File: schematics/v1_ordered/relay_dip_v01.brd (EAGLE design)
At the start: 50 x 50 mm, 49 parts, among them IC2 DS2432P

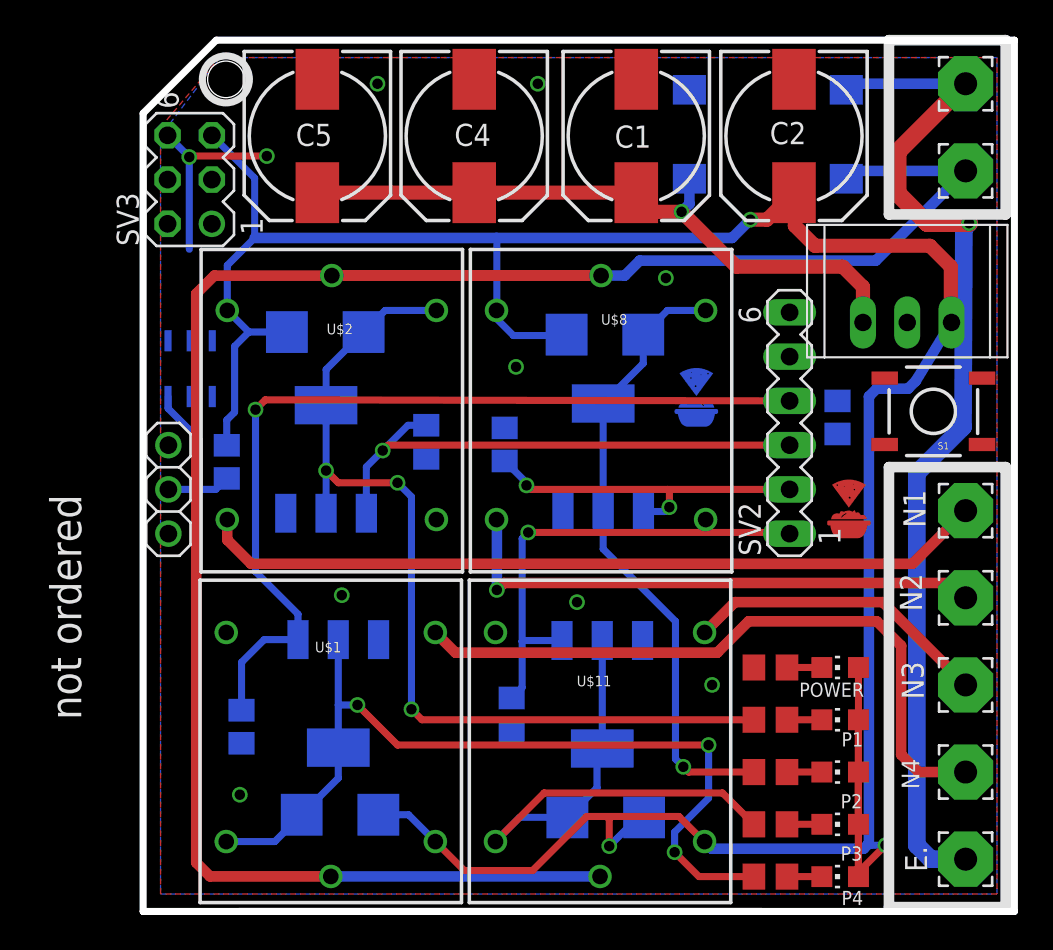
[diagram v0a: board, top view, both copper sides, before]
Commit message: moved files to subfolder
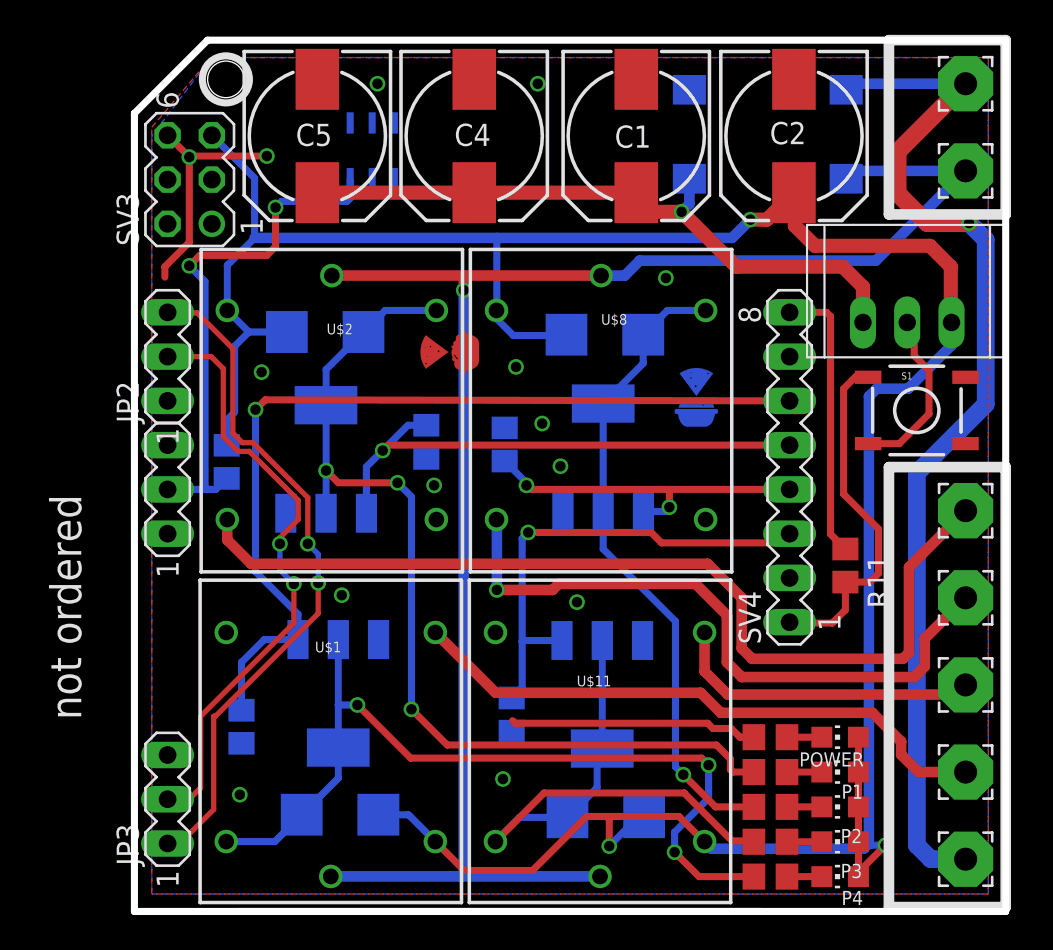
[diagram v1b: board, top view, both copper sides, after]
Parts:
- removed SV2: (no value), con-lstb:MA06-1
- added JP2, JP3: (no value), con-lstb:MA03-1
- added SV4: (no value), con-lstb:MA08-1
- JP1: device adafruit:1X03 -> con-lstb:MA03-1
- moved U$4 24.6 mm to (17.6, 32.1), turned to 90 degrees
- moved U$5 20.8 mm to (28.4, 48.0), turned to 270 degrees
- moved IC2 16.3 mm to (13.2, 43.6)
- moved R11 8.51 mm to (40.3, 19.9), flipped to the top, turned to 270 degrees
- moved POWER 4.00 mm to (40.0, 10.0)
- moved R7 4.00 mm to (36.0, 10.0)
- moved P1 3.00 mm to (40.0, 8.00)
- moved R3 3.00 mm to (36.0, 8.00)
- moved P2 2.00 mm to (40.0, 6.00)
- moved R4 2.00 mm to (36.0, 6.00)
- moved P3 1.00 mm to (40.0, 4.00)
- moved R5 1.00 mm to (36.0, 4.00)
- moved S1 0.95 mm to (44.4, 28.8), turned to 0 degrees
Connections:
- new net N$1: R11.2, S1.1, SV4.1
- new net N$6: R11.1, SV4.8
- new net SCL: JP2.2, JP3.2
- new net SDA: JP2.3, JP3.1
- net GND: now also JP3.3, S1.3
- net P0: now also SV4.6; no longer SV2.4
- net P2: now also SV4.5; no longer SV2.3
- net P4: now also SV4.4; no longer SV2.2
- net P6: now also SV4.3; no longer SV2.1
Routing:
- net SDA: track 0.00 -> 39.4 mm, vias 0 -> 2
- net SCL: track 0.00 -> 34.8 mm, vias 0 -> 2
- net PHASE: track 125.7 -> 95.9 mm, vias 0 -> 1
- net GND: track 11.6 -> 38.0 mm, vias 10 -> 14
- net VCC: track 185.2 -> 164.4 mm
- net LD2: track 9.67 -> 30.2 mm, vias 0 -> 2
- net N$1: track 0.00 -> 20.4 mm
- net N$6: track 0.00 -> 16.1 mm
- net NCL1: track 45.4 -> 54.5 mm
- net NCL2: track 31.5 -> 37.7 mm
- net NCL: track 38.9 -> 34.2 mm
- net RELAY_LO1: track 53.7 -> 55.3 mm
- net RELAY_LO2: track 36.0 -> 37.1 mm
- net EARTH: track 59.8 -> 60.6 mm
- net RELAY_LO0: track 50.2 -> 49.5 mm
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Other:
- board text added: "JKW v0.1"
- board text added: "RELAY DIP I"
- board text removed: "CHIP bat connector"
- board text removed: "Input 5V Close left"
- board text removed: "JKW v0.32"
- board text removed: "ONION DIP IIb"

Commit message: v2
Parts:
- removed C1: EMVE500ADA221MJA0G, rcl:150CLZ-0810
- added IC1: 74HCT04D, 74xx-eu:SO14
- C2, C4, C5: value (none) -> EMZR500ADA221MHA0G
- moved U$5 46.9 mm to (41.5, 2.95), turned to 0 degrees
- moved R8 31.2 mm to (31.4, 28.1), turned to 90 degrees
- moved U$4 23.0 mm to (1.70, 15.6), turned to 0 degrees
- moved R6 17.2 mm to (33.4, 28.1)
- moved U$6 16.0 mm to (15.8, 29.0)
- moved C2 3.90 mm to (33.5, 44.5)
- moved C4 3.10 mm to (22.1, 44.5)
- moved E 1.00 mm to (46.2, 47.5)
- moved E. 1.00 mm to (46.2, 3.00)
- moved N1 1.00 mm to (46.2, 23.0)
- moved N2 1.00 mm to (46.2, 18.0)
- moved N3 1.00 mm to (46.2, 13.0)
- moved N4 1.00 mm to (46.2, 8.00)
- moved P 1.00 mm to (46.2, 42.5)
- moved C5 0.75 mm to (10.8, 44.5)
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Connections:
- removed net N$6: R11.1, SV4.8
- new net 3V: IC1.14, R10.1, R11.1, R6.1, R8.1, R9.1, SV4.8
- new net N$11: IC1.10, U$12.1
- new net N$2: IC1.2, U$3.1
- new net N$7: IC1.4, U$7.1
- new net N$9: IC1.6, U$9.1
- net GND: now also IC1.7; no longer C1.-, R10.2, R6.2, R8.2, R9.2
- net N$5: no longer C1.+
- net P0: now also IC1.1, R8.2; no longer R8.1, U$3.1
- net P2: now also IC1.3, R6.2; no longer R6.1, U$7.1
- net P4: now also IC1.5, R9.2; no longer R9.1, U$9.1
- net P6: now also IC1.11, R10.2; no longer R10.1, U$12.1
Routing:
- net 3V: track 0.00 -> 77.6 mm, vias 0 -> 3
- net N$11: track 0.00 -> 53.6 mm, vias 0 -> 2
- net N$2: track 0.00 -> 38.2 mm, vias 0 -> 2
- net P6: track 28.6 -> 66.0 mm
- net P0: track 51.6 -> 21.6 mm, vias 1 -> 2
- net N$7: track 0.00 -> 27.3 mm, vias 0 -> 2
- net N$9: track 0.00 -> 25.0 mm, vias 0 -> 2
- net P4: track 19.8 -> 42.3 mm
- net N$6: track 16.1 -> 0.00 mm
- net GND: track 38.0 -> 43.6 mm, vias 14 -> 16
- net VCC: track 164.4 -> 169.8 mm
- net PHASE: track 95.9 -> 101.3 mm, vias 1 -> 3
- net P2: track 30.6 -> 27.4 mm, vias 1 -> 2
- net NCL1: track 54.5 -> 52.7 mm
- net EARTH: track 60.6 -> 59.0 mm
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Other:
- board text added: "JKW v0.2"
- board text removed: "JKW v0.1"
- board text removed: "not ordered"
